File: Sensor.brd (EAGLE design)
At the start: 50.5 x 39.4 mm, 16 parts

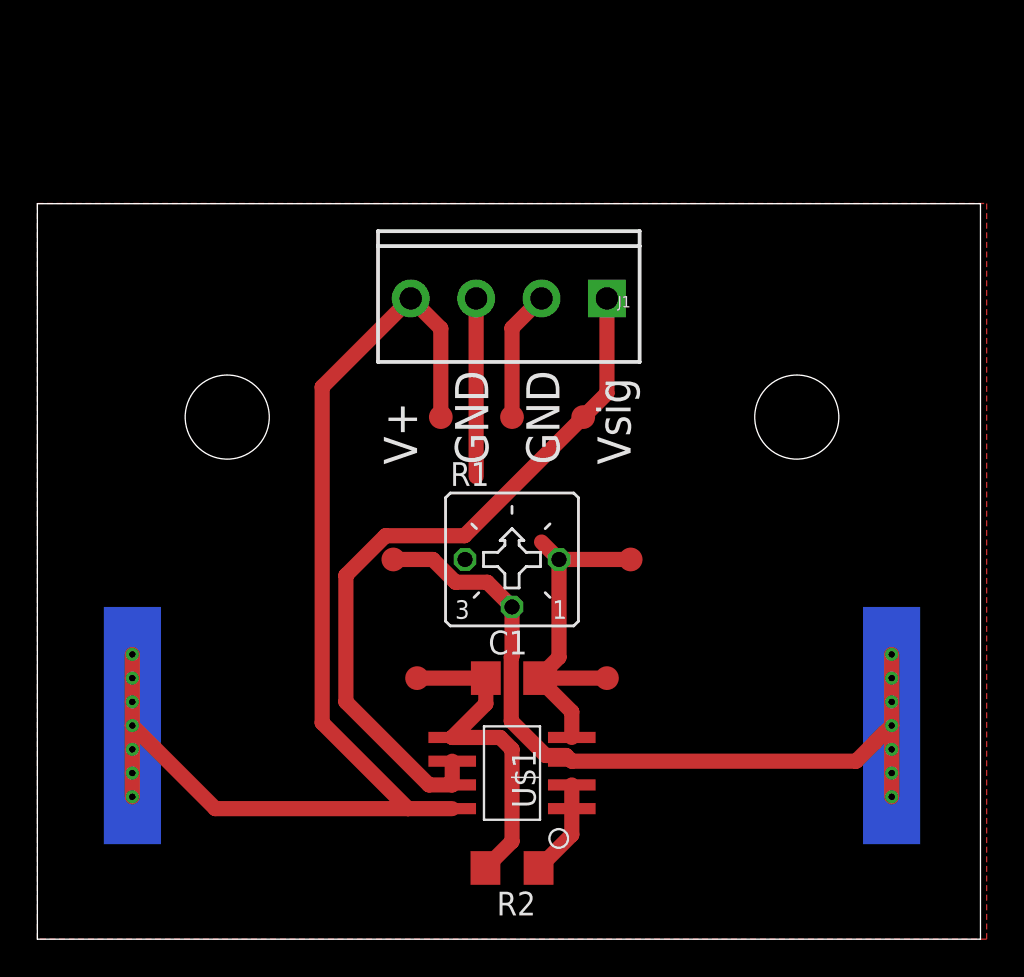
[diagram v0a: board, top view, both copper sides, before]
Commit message: Changed board dimensions
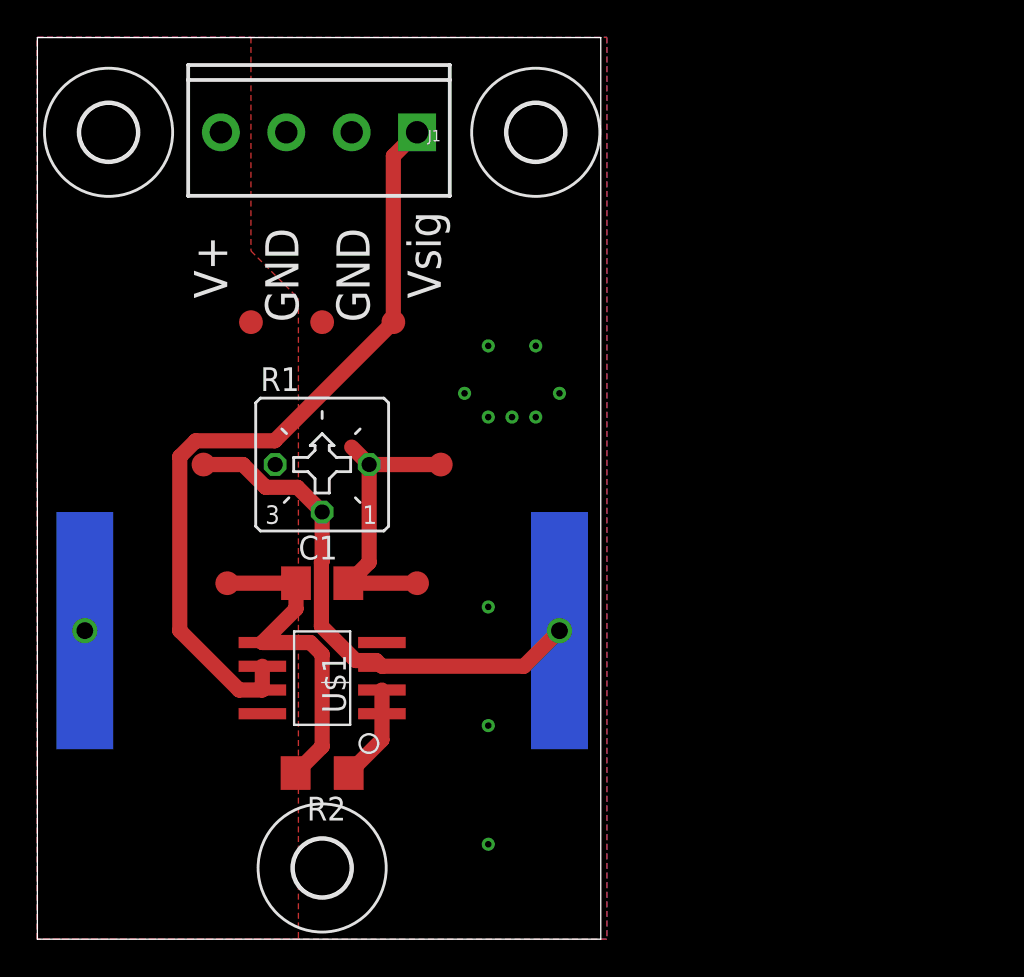
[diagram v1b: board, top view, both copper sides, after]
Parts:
- removed H2: MOUNT-HOLE-NPTH-M4, FormE:MOUNT-HOLE-M4
- added H3, H4: MOUNT-HOLE3.0, holes:3,0
- H1: value MOUNT-HOLE-NPTH-M4 -> MOUNT-HOLE3.0; device FormE:MOUNT-HOLE-M4 -> holes:3,0
- R1: value (none) -> 2M
- moved U$3 18.5 mm to (27.9, 16.5)
- moved H1 16.5 mm to (3.81, 43.2)
- moved J1 13.5 mm to (20.3, 43.2)
- moved TP1 11.4 mm to (10.2, 19.1)
- moved TP2 11.4 mm to (11.4, 33.0)
- moved TP5 11.4 mm to (19.1, 33.0)
- moved TP7 11.4 mm to (20.3, 19.1)
- moved C1 11.4 mm to (15.2, 19.1)
- moved R1 11.4 mm to (15.2, 25.4)
- moved R2 11.4 mm to (15.2, 8.89)
- moved TP3 11.4 mm to (21.6, 25.4)
- moved TP4 11.4 mm to (15.2, 33.0)
- moved TP6 11.4 mm to (8.89, 25.4)
- moved U$1 11.4 mm to (15.2, 14.0)
- moved U$2 5.68 mm to (2.54, 16.5)
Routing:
- net +3V3: track 64.8 -> 0.00 mm, vias 7 -> 1
- net GND: track 36.1 -> 15.6 mm, vias 0 -> 10
- net N$2: track 43.2 -> 27.9 mm, vias 7 -> 1
- net VSIG: track 38.7 -> 41.4 mm
- added copper zone on layer 1, net +3V3
- added copper zone on layer 16, net GND
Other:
- board size 50.5 x 39.4 mm -> 30.1 x 48.2 mm

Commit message: Added cart from digikey, updated schematic with values
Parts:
- C1: value (none) -> 10uF
- R2: value (none) -> 100k
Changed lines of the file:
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@@
 </autorouter>
 <elements>
-<element name="C1" library="rcl" library_urn="urn:adsk.eagle:library:334" package="C1206" package3d_urn="urn:adsk.eagle:package:23618/2" value="" x="15.24" y="19.05" smashed="yes">
+<element name="C1" library="rcl" library_urn="urn:adsk.eagle:library:334" package="C1206" package3d_urn="urn:adsk.eagle:package:23618/2" value="10uF" x="15.24" y="19.05" smashed="yes">
 <attribute name="NAME" x="13.97" y="20.32" size="1.27" layer="25"/>
 <attribute name="POPULARITY" value="24" x="46.99" y="-6.35" size="1.778" layer="27" display="off"/>
@@
 <attribute name="VALUE" x="11.9634" y="20.193" size="1.27" layer="27" ratio="10"/>
 </element>
-<element name="R2" library="rcl" library_urn="urn:adsk.eagle:library:334" package="R1206" package3d_urn="urn:adsk.eagle:package:23540/2" value="" x="15.24" y="8.89" smashed="yes" rot="R180">
+<element name="R2" library="rcl" library_urn="urn:adsk.eagle:library:334" package="R1206" package3d_urn="urn:adsk.eagle:package:23540/2" value="100k" x="15.24" y="8.89" smashed="yes" rot="R180">
 <attribute name="NAME" x="16.51" y="7.62" size="1.27" layer="25" rot="R180"/>
 <attribute name="POPULARITY" value="19" x="0" y="41.91" size="1.778" layer="27" rot="R180" display="off"/>
